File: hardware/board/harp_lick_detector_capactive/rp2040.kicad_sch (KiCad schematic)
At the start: 37 parts, among them J2 USB_C_Receptacle_USB2.0, U7 W25Q128JVS, U8 RP2040, X2 ECS-TXO-2016

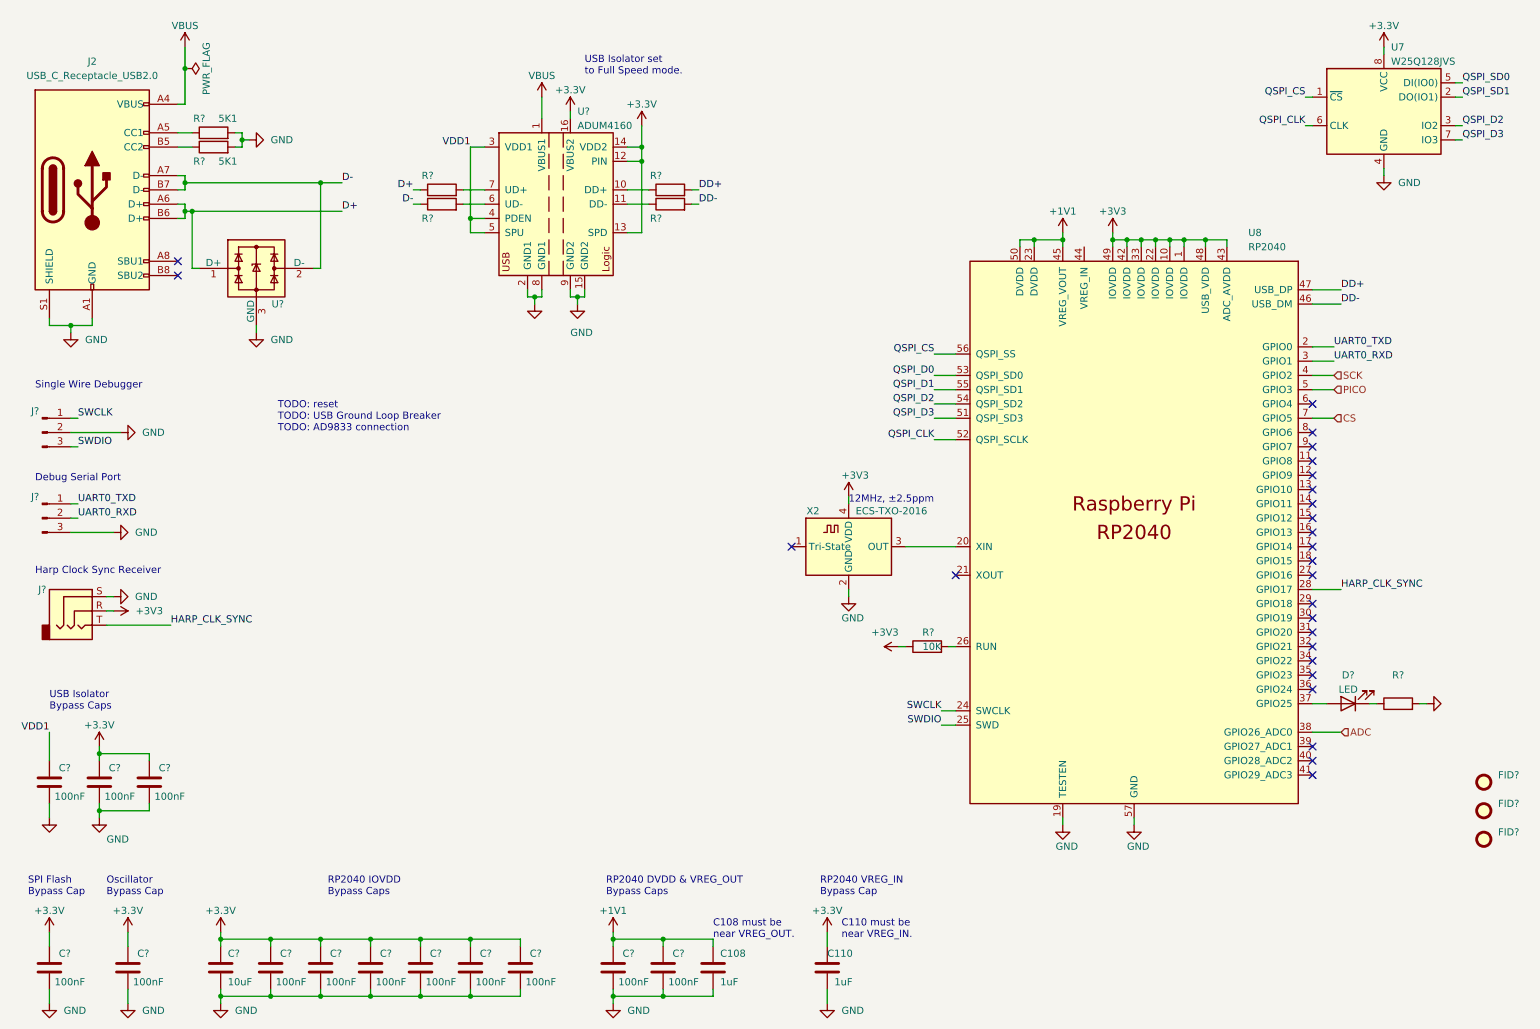
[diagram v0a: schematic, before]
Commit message: add ttl output; update adc voltage
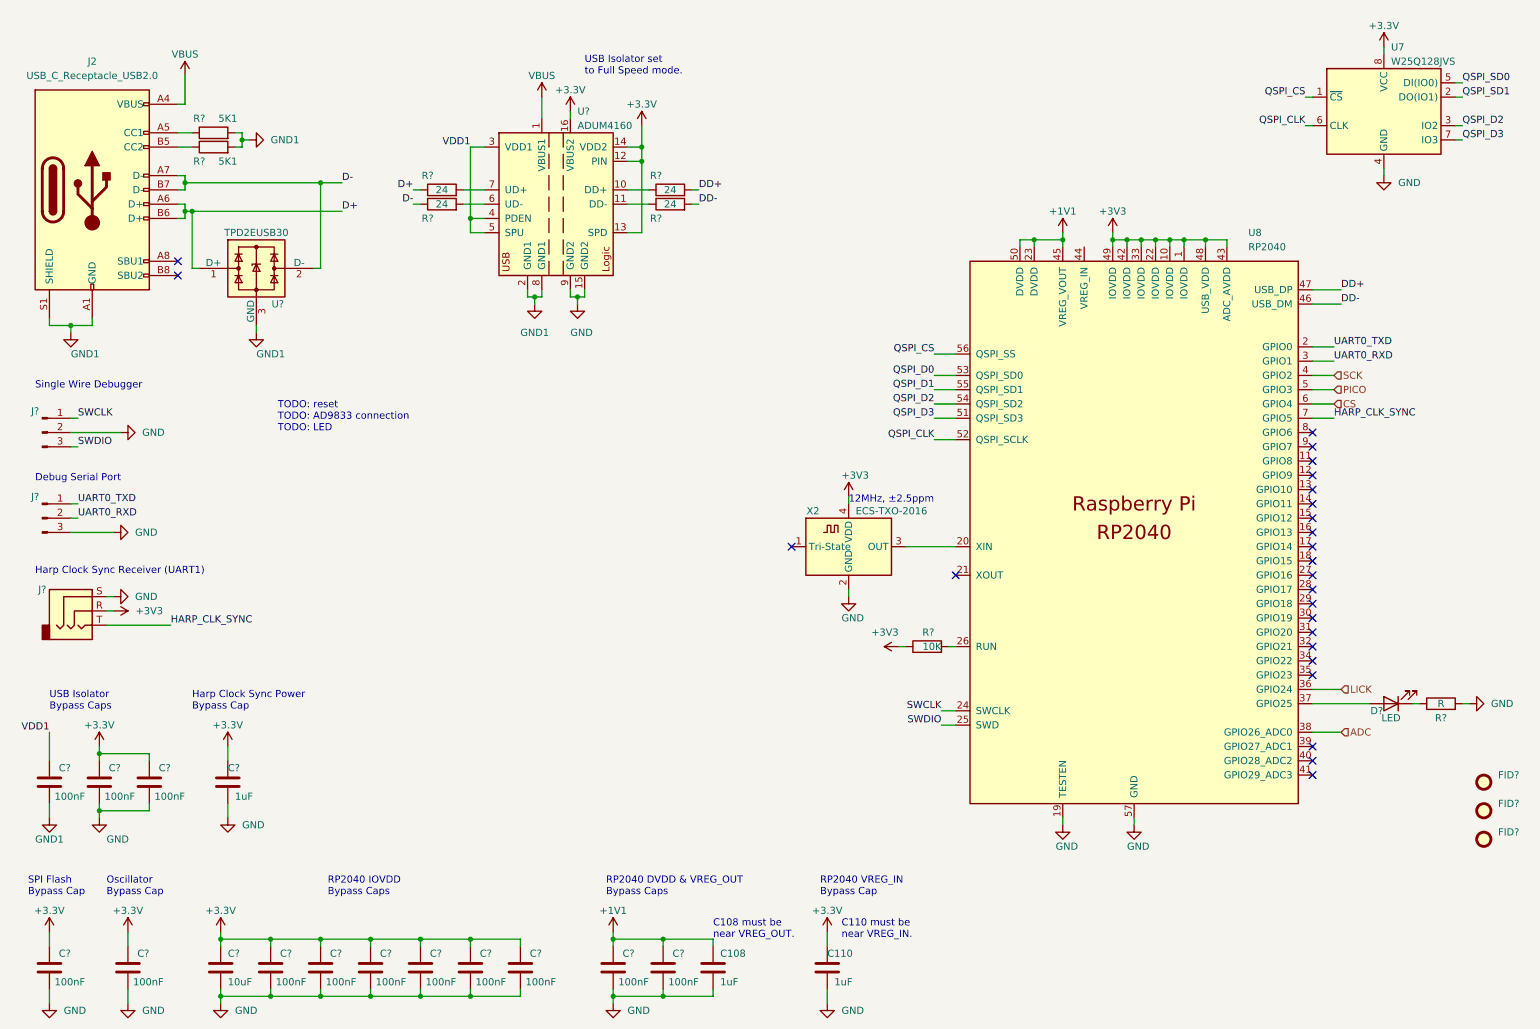
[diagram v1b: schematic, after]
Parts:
- added C?: 1uF, Capacitor_SMD:C_0603_1608Metric_Pad1.08x0.95mm_HandSolder, symbol Device:C
- R?: value (none) -> R
- R? (x4): value (none) -> 24
- U?: value (none) -> TPD2EUSB30; footprint (none) -> Package_TO_SOT_SMD:Texas_DRT-3
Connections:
- net +3V3: now also C?.1
- net CS: now also U8.6 (GPIO4); no longer U8.7 (GPIO5)
- net GND: now also C?.2; no longer J2.A1 (GND), J2.A12 (GND), J2.B1 (GND), J2.B12 (GND), J2.S1 (SHIELD), R?.2, R?.2, U?.3 (GND)
- net GND1: now also J2.A1 (GND), J2.A12 (GND), J2.B1 (GND), J2.B12 (GND), J2.S1 (SHIELD), R?.2, R?.2, U?.3 (GND)
- net HARP_CLK_SYNC: now also U8.7 (GPIO5); no longer U8.28 (GPIO17)
- net LICK: now reaches U8.36 (GPIO24)
- no-connect marks 26 -> 25
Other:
- note added: "Harp Clock Sync Power Bypass Cap"
- note added: "Harp Clock Sync Receiver (UART1)"
- note added: "TODO: reset TODO: AD9833 connection TODO: LED"
- note removed: "Harp Clock Sync Receiver"
- note removed: "TODO: reset TODO: USB Ground Loop Breaker TODO: AD9833 connection"
- moved on the sheet: D?, R?

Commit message: add extra series termination resistors
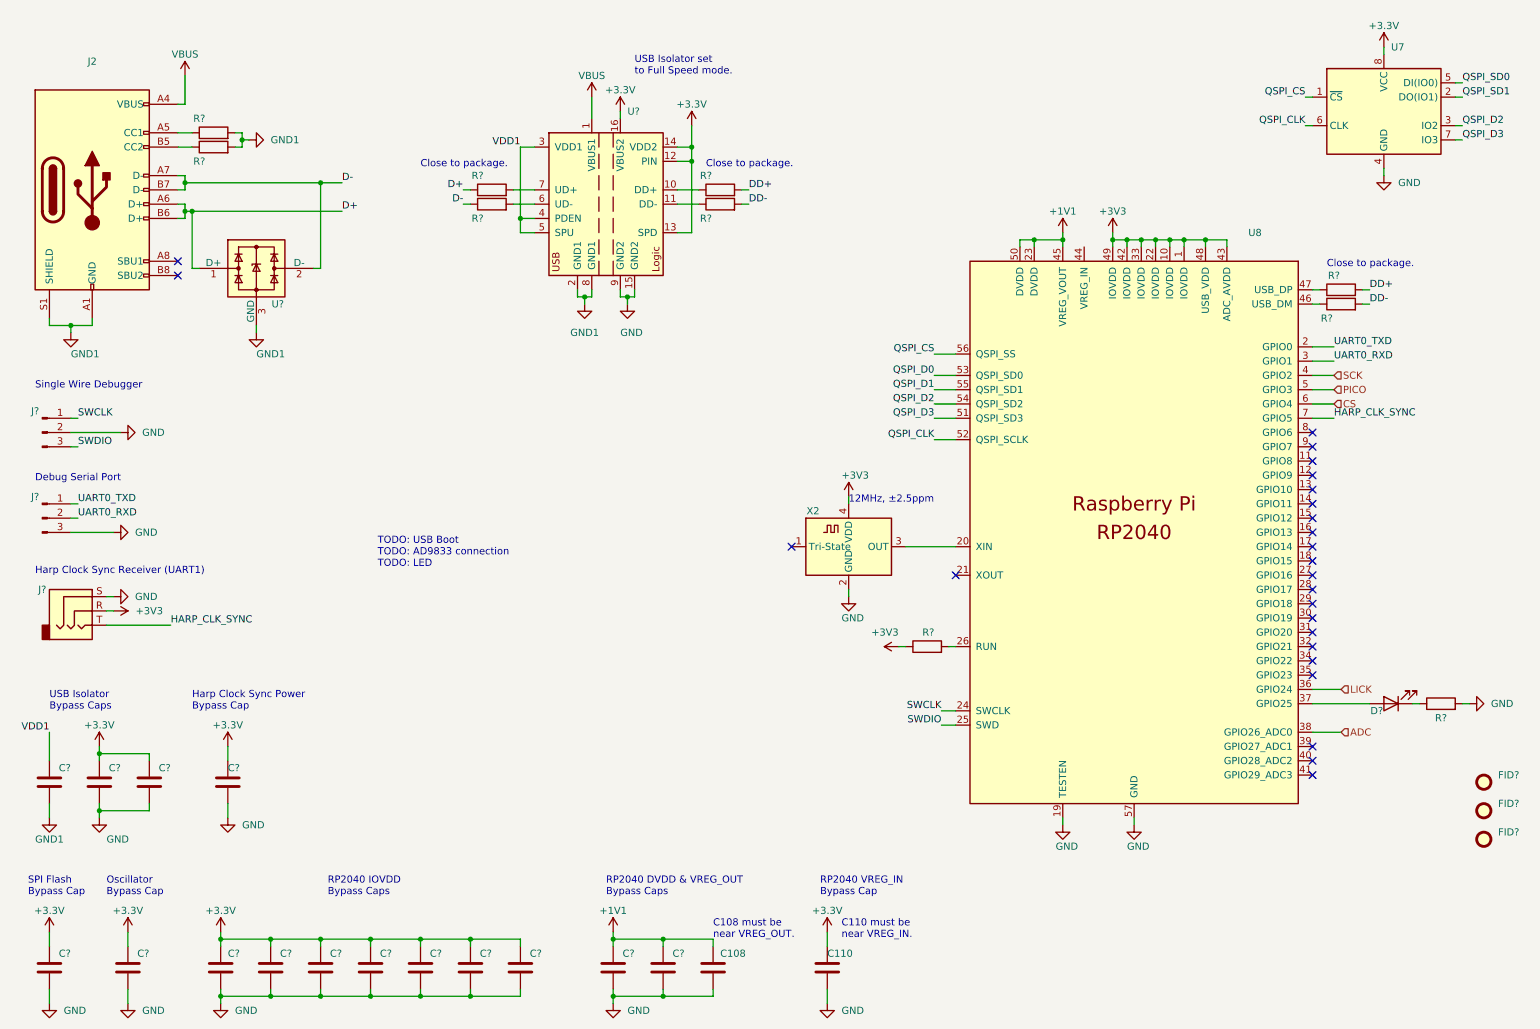
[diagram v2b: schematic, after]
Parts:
- added R? (x2): (no value), symbol Device:R
- C108, C110, C?: value 1uF -> (none); footprint Capacitor_SMD:C_0603_1608Metric_Pad1.08x0.95mm_HandSolder -> (none)
- C? (x13): value 100nF -> (none); footprint Capacitor_SMD:C_0603_1608Metric_Pad1.08x0.95mm_HandSolder -> (none)
- C?: value 10uF -> (none); footprint Capacitor_SMD:C_0805_2012Metric -> (none)
- D?: value LED -> (none)
- FID? (x2): value ~ -> (none); footprint Fiducial:Fiducial_0.5mm_Mask1mm -> (none)
- FID?: value Fiducial -> (none); footprint Fiducial:Fiducial_0.5mm_Mask1mm -> (none)
- J2: value USB_C_Receptacle_USB2.0 -> (none); footprint Connector_USB:USB_C_Receptacle_Amphenol_12401610E4-2A_CircularHoles -> (none)
- J?: value AudioJack3 -> (none)
- J?: value Conn_01x03_Male -> (none)
- J?: value ~ -> (none)
- R? (x2): value 5K1 -> (none); footprint Resistor_SMD:R_0603_1608Metric_Pad0.98x0.95mm_HandSolder -> (none)
- R?: value R -> (none)
- R? (x4): value 24 -> (none)
- R?: value 10K -> (none); footprint Resistor_SMD:R_0402_1005Metric_Pad0.72x0.64mm_HandSolder -> (none)
- U7: value W25Q128JVS -> (none); footprint Package_SO:SOIC-8_5.23x5.23mm_P1.27mm -> (none)
- U8: value RP2040 -> (none); footprint RP2040_minimal:RP2040-QFN-56 -> (none)
- U?: value ADUM4160 -> (none); footprint Package_SO:SOIC-16W_7.5x10.3mm_P1.27mm -> (none)
- U?: value TPD2EUSB30 -> (none); footprint Package_TO_SOT_SMD:Texas_DRT-3 -> (none)
- X2: value ECS-TXO-2016 -> (none); footprint Crystal:Crystal_SMD_2016-4Pin_2.0x1.6mm -> (none)
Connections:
- net DD+: now also R?.2; no longer U8.47 (USB_DP)
- net DD-: now also R?.2; no longer U8.46 (USB_DM)
- new net: R?.1, U8.47 (USB_DP)
- new net: R?.1, U8.46 (USB_DM)
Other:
- note added: "Close to package."
- note added: "TODO: USB Boot TODO: AD9833 connection TODO: LED"
- note removed: "TODO: reset TODO: AD9833 connection TODO: LED"
- moved on the sheet: R?, U?

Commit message: add driven shield
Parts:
- C108, C110, C?: value (none) -> 1uF; footprint (none) -> Capacitor_SMD:C_0603_1608Metric_Pad1.08x0.95mm_HandSolder
- C? (x13): value (none) -> 100nF; footprint (none) -> Capacitor_SMD:C_0603_1608Metric_Pad1.08x0.95mm_HandSolder
- C?: value (none) -> 10uF; footprint (none) -> Capacitor_SMD:C_0805_2012Metric
- D?: value (none) -> LED
- FID? (x2): value (none) -> ~; footprint (none) -> Fiducial:Fiducial_0.5mm_Mask1mm
- FID?: value (none) -> Fiducial; footprint (none) -> Fiducial:Fiducial_0.5mm_Mask1mm
- J2: value (none) -> USB_C_Receptacle_USB2.0; footprint (none) -> Connector_USB:USB_C_Receptacle_Amphenol_12401610E4-2A_CircularHoles
- J?: value (none) -> AudioJack3
- J?: value (none) -> Conn_01x03_Male
- J?: value (none) -> ~
- R? (x2): value (none) -> 5K1; footprint (none) -> Resistor_SMD:R_0603_1608Metric_Pad0.98x0.95mm_HandSolder
- R? (x2): value (none) -> 27; footprint (none) -> Resistor_SMD:R_0603_1608Metric_Pad0.98x0.95mm_HandSolder
- R?: value (none) -> R
- R? (x4): value (none) -> 24
- R?: value (none) -> 10K; footprint (none) -> Resistor_SMD:R_0402_1005Metric_Pad0.72x0.64mm_HandSolder
- U7: value (none) -> W25Q128JVS; footprint (none) -> Package_SO:SOIC-8_5.23x5.23mm_P1.27mm
- U8: value (none) -> RP2040; footprint (none) -> RP2040_minimal:RP2040-QFN-56
- U?: value (none) -> ADUM4160; footprint (none) -> Package_SO:SOIC-16W_7.5x10.3mm_P1.27mm
- U?: value (none) -> TPD2EUSB30; footprint (none) -> Package_TO_SOT_SMD:Texas_DRT-3
- X2: value (none) -> ECS-TXO-2016; footprint (none) -> Crystal:Crystal_SMD_2016-4Pin_2.0x1.6mm

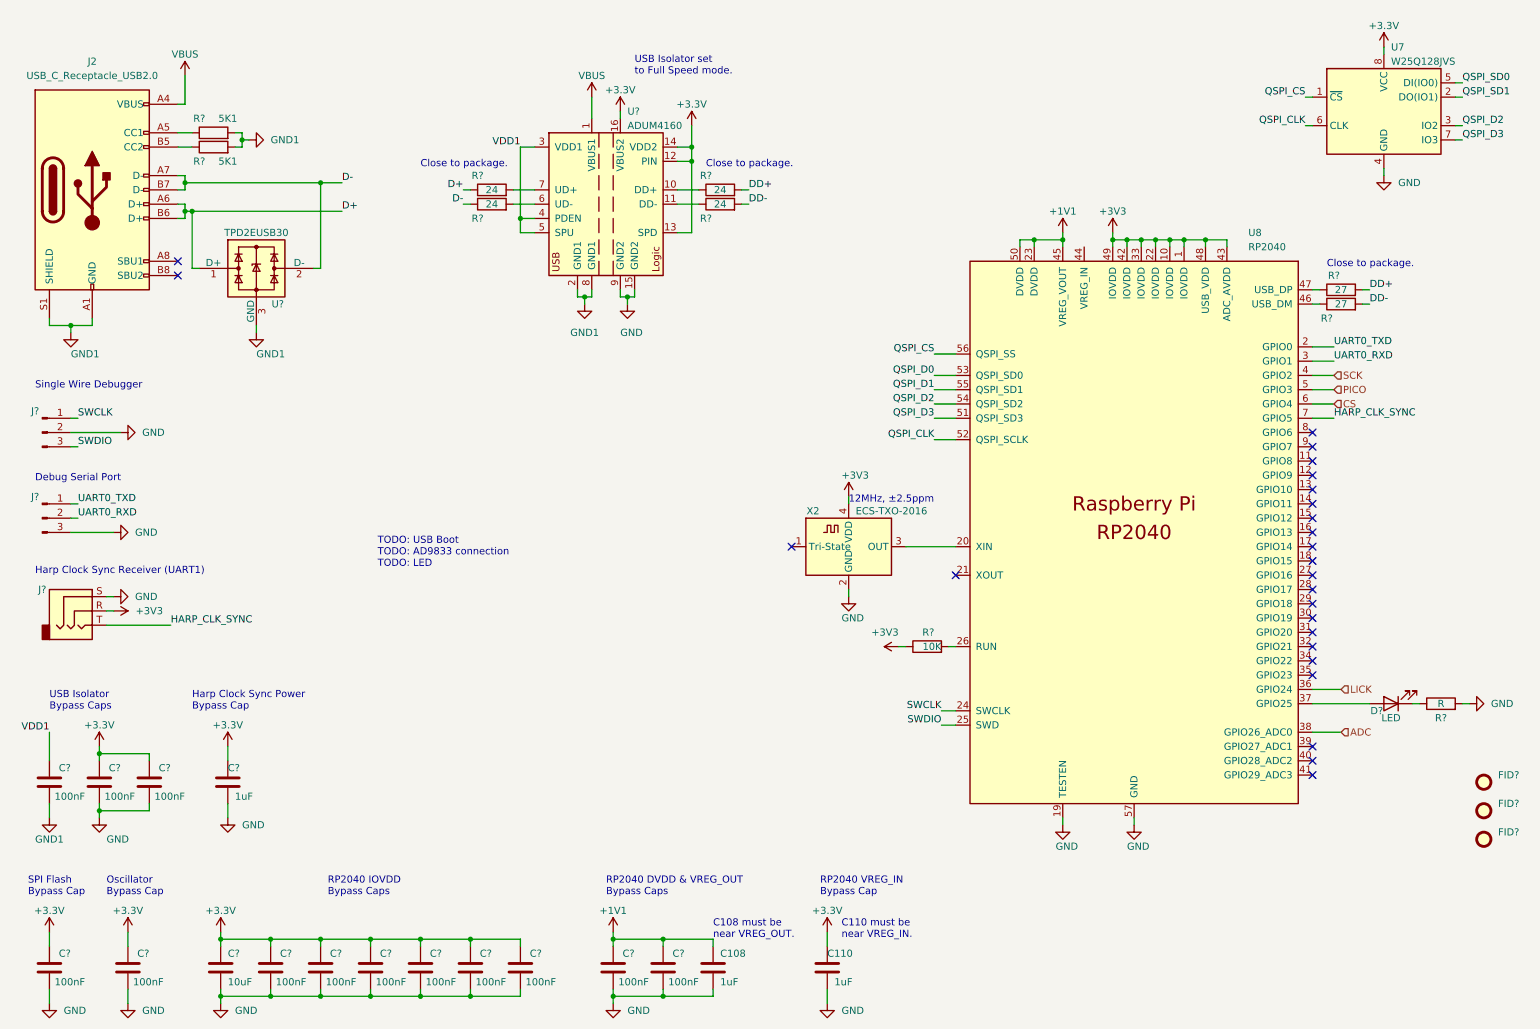
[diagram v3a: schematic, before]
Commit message: document stray capacitances
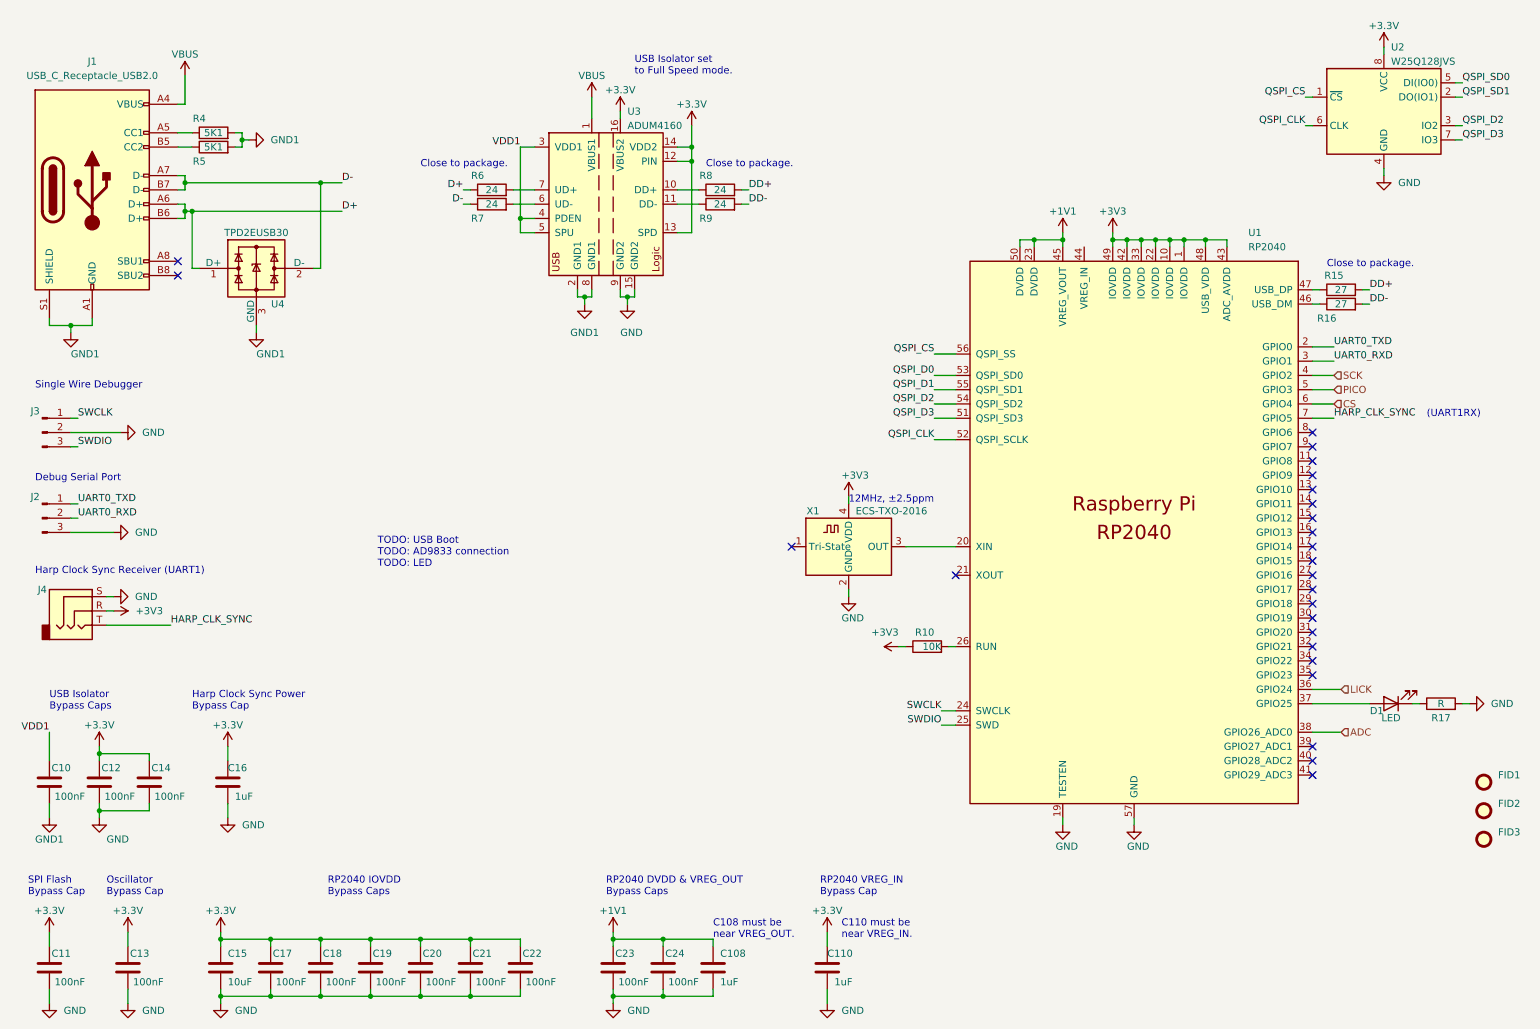
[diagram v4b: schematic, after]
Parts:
- gave numbers to parts that had none: 34
- renumbered J2 to J1, U8 to U1, U7 to U2, X2 to X1
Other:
- note added: "(UART1RX)"
